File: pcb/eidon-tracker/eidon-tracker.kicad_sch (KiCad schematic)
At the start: 9 parts, among them SW1 SW_SPDT, SW2 SW_Push, U1 XIAO-ESP32C6, U2 GY-BNO085

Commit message: feat(pcb): adds BOM and pick-n-place pos files needed for PCBA
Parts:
- BT1: Manufacturer Part Number (MPN) (none) -> JST S2B-PH-K-S(LF)(SN); Supplier & Ref (none) -> Digi-Key 455-S2B-PH-K
- D1: Manufacturer Part Number (MPN) (none) -> Kingbright APT2012YC; Supplier & Ref (none) -> Digi-Key 754-1121-1-ND
- R1, R2: Manufacturer Part Number (MPN) (none) -> Yageo RC0805FR-07220KL; Supplier & Ref (none) -> LCSC C25811
- R3: Manufacturer Part Number (MPN) (none) -> Yageo RC0805FR-071K8L; Supplier & Ref (none) -> LCSC C22807
- SW1: Manufacturer Part Number (MPN) (none) -> CK OS102011MA1Q; Supplier & Ref (none) -> Mouser 611-OS102011MA1Q
- SW2: Manufacturer Part Number (MPN) (none) -> Alps SKRKACE010; Supplier & Ref (none) -> Mouser 688-SKRKACE010
- U1: value XIAO-ESP32C6 -> XIAO-ESP32-C6; Manufacturer Part Number (MPN) (none) -> Seeed 113991114; Supplier & Ref (none) -> Seeed / Digi-Key; now left out of the parts list
- U2: Manufacturer Part Number (MPN) (none) -> GY-BNO085; Supplier & Ref (none) -> Amazon / AliExpress; now left out of the parts list
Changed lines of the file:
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@@
 		(unit 1)
 		(exclude_from_sim no)
-		(in_bom yes)
-		(on_board yes)
+		(in_bom no)
+		(on_board no)
 		(dnp no)
 		(property "Reference" "U1"
@@
 			)
 		)
-		(property "Value" "XIAO-ESP32C6"
+		(property "Value" "XIAO-ESP32-C6"
 			(at 90.424 91.948 0)
 			(effects
@@
 		)
 		(property "Description" ""
+			(at 86.36 68.58 0)
+			(effects
+				(font
+					(size 1.27 1.27)
+				)
+				(hide yes)
+			)
+		)
+		(property "Manufacturer Part Number (MPN)" "Seeed 113991114"
+			(at 86.36 68.58 0)
+			(effects
+				(font
+					(size 1.27 1.27)
+				)
+				(hide yes)
+			)
+		)
+		(property "Supplier & Ref" "Seeed / Digi-Key"
 			(at 86.36 68.58 0)
 			(effects
@@
 			)
 		)
-		(property "Datasheet" "~"
+		(property "Datasheet" ""
 			(at 149.86 132.08 0)
 			(effects
@@
 			)
 		)
+		(property "Manufacturer Part Number (MPN)" "Yageo RC0805FR-07220KL"
+			(at 149.86 132.08 0)
+			(effects
+				(font
+					(size 1.27 1.27)
+				)
+				(hide yes)
+			)
+		)
+		(property "Supplier & Ref" "LCSC C25811"
+			(at 149.86 132.08 0)
+			(effects
+				(font
+					(size 1.27 1.27)
+				)
+				(hide yes)
+			)
+		)
 		(pin "1"
 		)
@@
 			)
 		)
-		(property "Datasheet" "~"
+		(property "Datasheet" ""
 			(at 149.86 142.24 0)
 			(effects
@@
 		)
 		(property "Description" "Resistor"
+			(at 149.86 142.24 0)
+			(effects
+				(font
+					(size 1.27 1.27)
+				)
+				(hide yes)
+			)
+		)
+		(property "Manufacturer Part Number (MPN)" "Yageo RC0805FR-07220KL"
+			(at 149.86 142.24 0)
+			(effects
+				(font
+					(size 1.27 1.27)
+				)
+				(hide yes)
+			)
+		)
+		(property "Supplier & Ref" "LCSC C25811"
 			(at 149.86 142.24 0)
 			(effects
@@
 			)
 		)
+		(property "Manufacturer Part Number (MPN)" "CK OS102011MA1Q"
+			(at 101.6 137.16 0)
+			(effects
+				(font
+					(size 1.27 1.27)
+				)
+				(hide yes)
+			)
+		)
+		(property "Supplier & Ref" "Mouser 611-OS102011MA1Q"
+			(at 101.6 137.16 0)
+			(effects
+				(font
+					(size 1.27 1.27)
+				)
+				(hide yes)
+			)
+		)
 		(pin "3"
 		)
@@
 			)
 		)
-		(property "Datasheet" "~"
+		(property "Datasheet" ""
 			(at 248.92 137.16 0)
 			(effects
@@
 			)
 		)
-		(property "Description" "Light emitting diode"
+		(property "Description" "Yellow LED, 0805, common cathode"
 			(at 248.92 137.16 0)
 			(effects
@@
 		)
 		(property "Sim.Pins" "1=K 2=A"
+			(at 248.92 137.16 0)
+			(effects
+				(font
+					(size 1.27 1.27)
+				)
+				(hide yes)
+			)
+		)
+		(property "Manufacturer Part Number (MPN)" "Kingbright APT2012YC"
+			(at 248.92 137.16 0)
+			(effects
+				(font
+					(size 1.27 1.27)
+				)
+				(hide yes)
+			)
+		)
+		(property "Supplier & Ref" "Digi-Key 754-1121-1-ND"
 			(at 248.92 137.16 0)
 			(effects
@@
 			)
 		)
+		(property "Manufacturer Part Number (MPN)" "Alps SKRKACE010"
+			(at 196.85 137.16 0)
+			(effects
+				(font
+					(size 1.27 1.27)
+				)
+				(hide yes)
+			)
+		)
+		(property "Supplier & Ref" "Mouser 688-SKRKACE010"
+			(at 196.85 137.16 0)
+			(effects
+				(font
+					(size 1.27 1.27)
+				)
+				(hide yes)
+			)
+		)
 		(pin "2"
 		)
@@
 		(unit 1)
 		(exclude_from_sim no)
-		(in_bom yes)
-		(on_board yes)
+		(in_bom no)
+		(on_board no)
 		(dnp no)
 		(property "Reference" "U2"
@@
 			)
 		)
-		(property "Description" ""
+		(property "Description" "Teyleten Robot GY- BNO085"
 			(at 212.09 67.31 0)
 			(effects
@@
 				)
 				(hide yes)
+			)
+		)
+		(property "Manufacturer Part Number (MPN)" "GY-BNO085"
+			(at 212.09 67.31 0)
+			(effects
+				(font
+					(size 1.27 1.27)
+				)
+				(hide yes)
+			)
+		)
+		(property "Supplier & Ref" "Amazon / AliExpress"
+			(at 212.09 67.31 0)
+			(effects
+				(font
+					(size 1.27 1.27)
+				)
 			)
 		)
@@
 			)
 		)
+		(property "Manufacturer Part Number (MPN)" "JST S2B-PH-K-S(LF)(SN)"
+			(at 54.61 138.43 0)
+			(effects
+				(font
+					(size 1.27 1.27)
+				)
+				(hide yes)
+			)
+		)
+		(property "Supplier & Ref" "Digi-Key 455-S2B-PH-K"
+			(at 54.61 138.43 0)
+			(effects
+				(font
+					(size 1.27 1.27)
+				)
+				(hide yes)
+			)
+		)
 		(pin "1"
 		)
@@
 			)
 		)
-		(property "Datasheet" "~"
+		(property "Datasheet" ""
 			(at 240.03 137.16 0)
 			(effects
@@
 			(at 240.03 137.16 0)
 			(effects
+				(font
+					(size 1.27 1.27)
+				)
+				(hide yes)
+			)
+		)
+		(property "Manufacturer Part Number (MPN)" "Yageo RC0805FR-071K8L"
+			(at 240.03 137.16 0)
+			(effects
+				(font
+					(size 1.27 1.27)
+				)
+				(hide yes)
+			)
+		)
+		(property "Supplier & Ref" "LCSC C22807"
+			(at 240.03 137.16 0)
+			(effects

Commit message: feat(firmware/pcb): add status LED and battery monitoring
Firmware Changes:
- Add second status LED on GPIO1/A1 (blinks when scanning, solid when paired)
- Onboard LED now correctly uses GPIO15 for Seeed XIAO ESP32C6
- Implement battery voltage monitoring on GPIO0/A0 following official Seeed wiki
  * Uses analogReadMilliVolts() with 16-sample averaging
  * 1:2 voltage divider circuit (200k resistor)
  * Battery range: 4.2V (100%) to 3.0V (0%)
- Add battery presence detection to handle floating ADC when USB-only powered
  * Detects when no battery connected (prevents false 80% reading)
  * Reports 0% when USB powered without battery
- Battery readings every 5 seconds with detailed debug logging
- LED test code commented out but preserved for future hardware debugging

PCB Changes:
- Update schematic with blue status LED on GPIO1
- Correct resistor values for proper LED brightness in production
- Ensure next PCB batch will work with same firmware code

Hardware Notes:
- Current prototype has high-value resistor causing dim LED
- Next batch will have corrected resistor for proper brightness
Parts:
- D1: Manufacturer Part Number (MPN) Kingbright APT2012YC -> Kingbright APT2012QBC/D; Supplier & Ref Digi-Key 754-1121-1-ND -> Digi-Key 754-1137-1-ND
- R3: value 1.8k -> 330 Ω, 1%; Manufacturer Part Number (MPN) Yageo RC0805FR-071K8L -> Yageo RC0805FR-07330RL; Supplier & Ref LCSC C22807 -> Digi-Key 311-330CRCT-ND
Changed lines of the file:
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@@
 			)
 		)
-		(property "Description" "Yellow LED, 0805, common cathode"
+		(property "Description" "Very common high-eff blue"
 			(at 248.92 137.16 0)
 			(effects
@@
 			)
 		)
-		(property "Manufacturer Part Number (MPN)" "Kingbright APT2012YC"
+		(property "Manufacturer Part Number (MPN)" "Kingbright APT2012QBC/D"
 			(at 248.92 137.16 0)
 			(effects
@@
 			)
 		)
-		(property "Supplier & Ref" "Digi-Key 754-1121-1-ND"
+		(property "Supplier & Ref" "Digi-Key 754-1137-1-ND"
 			(at 248.92 137.16 0)
 			(effects
@@
 			)
 		)
-		(property "Value" "1.8k"
+		(property "Value" "330 Ω, 1%"
 			(at 240.03 139.7 90)
 			(effects
@@
 			)
 		)
-		(property "Manufacturer Part Number (MPN)" "Yageo RC0805FR-071K8L"
+		(property "Manufacturer Part Number (MPN)" "Yageo RC0805FR-07330RL"
 			(at 240.03 137.16 0)
 			(effects
@@
 			)
 		)
-		(property "Supplier & Ref" "LCSC C22807"
+		(property "Supplier & Ref" "Digi-Key 311-330CRCT-ND"
 			(at 240.03 137.16 0)
 			(effects

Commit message: revert: remove PCB LED and resistor changes
Revert PCB schematic changes from previous commit while keeping
firmware changes intact. The LED circuit and resistor value updates
will be applied in a future PCB revision.
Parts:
- D1: Manufacturer Part Number (MPN) Kingbright APT2012QBC/D -> Kingbright APT2012YC; Supplier & Ref Digi-Key 754-1137-1-ND -> Digi-Key 754-1121-1-ND
- R3: value 330 Ω, 1% -> 1.8k; Manufacturer Part Number (MPN) Yageo RC0805FR-07330RL -> Yageo RC0805FR-071K8L; Supplier & Ref Digi-Key 311-330CRCT-ND -> LCSC C22807
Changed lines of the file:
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@@
 			)
 		)
-		(property "Description" "Very common high-eff blue"
+		(property "Description" "Yellow LED, 0805, common cathode"
 			(at 248.92 137.16 0)
 			(effects
@@
 			)
 		)
-		(property "Manufacturer Part Number (MPN)" "Kingbright APT2012QBC/D"
+		(property "Manufacturer Part Number (MPN)" "Kingbright APT2012YC"
 			(at 248.92 137.16 0)
 			(effects
@@
 			)
 		)
-		(property "Supplier & Ref" "Digi-Key 754-1137-1-ND"
+		(property "Supplier & Ref" "Digi-Key 754-1121-1-ND"
 			(at 248.92 137.16 0)
 			(effects
@@
 			)
 		)
-		(property "Value" "330 Ω, 1%"
+		(property "Value" "1.8k"
 			(at 240.03 139.7 90)
 			(effects
@@
 			)
 		)
-		(property "Manufacturer Part Number (MPN)" "Yageo RC0805FR-07330RL"
+		(property "Manufacturer Part Number (MPN)" "Yageo RC0805FR-071K8L"
 			(at 240.03 137.16 0)
 			(effects
@@
 			)
 		)
-		(property "Supplier & Ref" "Digi-Key 311-330CRCT-ND"
+		(property "Supplier & Ref" "LCSC C22807"
 			(at 240.03 137.16 0)
 			(effects

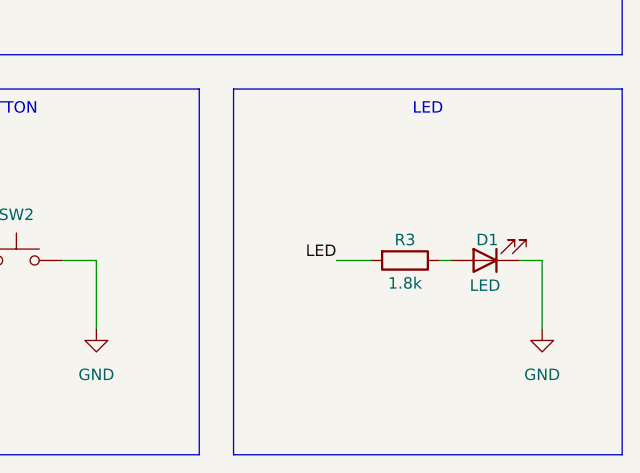
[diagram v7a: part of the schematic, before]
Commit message: feat(pcb): updates pcb BOM to have correct resistor value for desired LED brightness
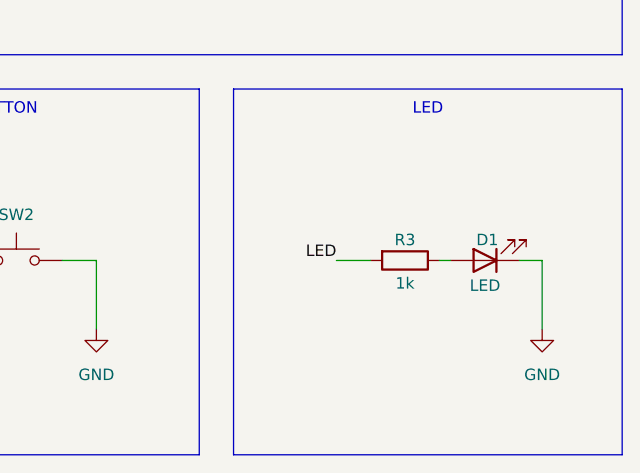
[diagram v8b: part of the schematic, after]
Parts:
- R3: value 1.8k -> 1k; Manufacturer Part Number (MPN) Yageo RC0805FR-071K8L -> Yageo RC0805FR-071KL; Supplier & Ref LCSC C22807 -> LCSC C95781; Digi-Key 311-1.00KCRCT-ND
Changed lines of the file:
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@@
 			)
 		)
-		(property "Value" "1.8k"
+		(property "Value" "1k"
 			(at 240.03 139.7 90)
 			(effects
@@
 			)
 		)
-		(property "Manufacturer Part Number (MPN)" "Yageo RC0805FR-071K8L"
+		(property "Manufacturer Part Number (MPN)" "Yageo RC0805FR-071KL"
 			(at 240.03 137.16 0)
 			(effects
@@
 			)
 		)
-		(property "Supplier & Ref" "LCSC C22807"
+		(property "Supplier & Ref" "LCSC C95781; Digi-Key 311-1.00KCRCT-ND"
 			(at 240.03 137.16 0)
 			(effects
